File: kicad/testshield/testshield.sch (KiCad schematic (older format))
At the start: 6 parts, among them J1 ISP header, J2 Raspiheader, SW1 SW_Push, U1 ATMEGA328P-PU

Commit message: update
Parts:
- R1: footprint Resistors_THT:R_Axial_DIN0207_L6.3mm_D2.5mm_P10.16mm_Horizontal -> Resistors_SMD:R_2010
- U1: footprint ATMEGA328P-PU:DIP794W46P254L2967H457Q28B -> ATMEGA328P-AU:QFP80P900X900X120-32N
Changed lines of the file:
@@
 F 0 "U1" H 3200 4600 50  0000 L BNN
 F 1 "ATMEGA328P-PU" H 4350 1950 50  0000 L BNN
-F 2 "ATMEGA328P-PU:DIP794W46P254L2967H457Q28B" H 3950 3350 50  0001 C CIN
+F 2 "ATMEGA328P-AU:QFP80P900X900X120-32N" H 3950 3350 50  0001 C CIN
 F 3 "" H 3950 3350 50  0001 C CNN
 	1    3950 3350
@@
 F 0 "R1" V 6130 3250 50  0000 C CNN
 F 1 "10k" V 6050 3250 50  0000 C CNN
-F 2 "Resistors_THT:R_Axial_DIN0207_L6.3mm_D2.5mm_P10.16mm_Horizontal" V 5980 3250 50  0001 C CNN
+F 2 "Resistors_SMD:R_2010" V 5980 3250 50  0001 C CNN
 F 3 "" H 6050 3250 50  0001 C CNN
 	1    6050 3250

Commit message: Add files via upload
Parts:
- removed J1: ISP header, Pin_Headers:Pin_Header_Straight_2x03_Pitch2.54mm, symbol Conn_02x03_Odd_Even
- removed R1: 10k, Resistors_SMD:R_2010, symbol R
- removed SW1: SW_Push, Buttons_Switches_SMD:SW_SPST_B3S-1000, symbol SW_Push
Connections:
- net +3V3: now also J2.17 (Pin_17); no longer J2.1 (Pin_1)
- net GNDD: now also J2.14 (Pin_14), J2.20 (Pin_20), J2.25 (Pin_25), J2.30 (Pin_30), J2.34 (Pin_34), J2.39 (Pin_39), J2.9 (Pin_9)
- net at U1.1 ((PCINT14/~RESET~)PC6): now also J2.26 (Pin_26)
- net at U1.16 ((PCINT2/OC1B/~SS~)PB2): now also J2.24 (Pin_24)
- net at U1.17 ((PCINT3/OC2A/MOSI)PB3): now also J2.19 (Pin_19)
- net at U1.18 ((PCINT4/MISO)PB4): now also J2.21 (Pin_21)
- net at U1.19 ((PCINT5/SCK)PB5): now also J2.23 (Pin_23)
- net at U1.2 ((PCINT16/RXD)PD0): now also J2.8 (Pin_8)
- net at U1.26 ((PCINT11/ADC3)PC3): now also J2.11 (Pin_11)
- net at U1.3 ((PCINT17/TXD)PD1): now also J2.10 (Pin_10)
- net at U1.5 ((PCINT19/OC2B/INT1)PD3): now also J2.32 (Pin_32)
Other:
- moved on the sheet: J2

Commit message: Add files via upload
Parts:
- added D1: LED1, LEDs:LED_0603, symbol LED
- added D2: LED2, LEDs:LED_0603, symbol LED
- added J1: ISP/PDI, Pin_Headers:Pin_Header_Straight_2x03_Pitch2.54mm, symbol Conn_02x03_Odd_Even
- added R1: 1k, Resistors_SMD:R_0603, symbol R
- added R2, R3: 330, Resistors_SMD:R_0603, symbol R
- added R4: 10k, Resistors_SMD:R_0603, symbol R
- added SW1: Reset, Buttons_Switches_SMD:SW_SPST_B3U-1000P, symbol SW_Push
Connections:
- wire segments 75 -> 99

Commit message: simplification of schema with labels, WIP
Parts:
- D1, D2: symbol LED -> LED-RESCUE-testshield
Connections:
- net labels added: 3V3, GND, MISO, MOSI, PWM, RST, RX, SCK, SCL, SDA, SS, TX
- wire segments 99 -> 75
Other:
- note added: "TX / RX based on Raspberry Pi pins"
- moved on the sheet: R2, R3, R4, SW1

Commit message: further simplification,  still WIP
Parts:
- added R? (x2): 2K7, symbol R
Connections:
- net +3V3: now also R?.1, R?.1
- net PWM: now also U1.24 ((PCINT9/ADC1)PC1)
- net SCL: now also R?.2
- net SDA: now also R?.2
- net GPIO23: now reaches U1.25 ((PCINT10/ADC2)PC2)
- net GPIO23: now also J2.16 (Pin_16)
- net GPIO17: now reaches J2.11 (Pin_11), U1.26 ((PCINT11/ADC3)PC3)
- net at U1.5 ((PCINT19/OC2B/INT1)PD3): no longer J2.32 (Pin_32)
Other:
- note added: "Power"
- note added: "Programming header"
- note added: "Pull-up resistors for i2c lines\n"
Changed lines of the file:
@@
 	-1   0    0    1
 $EndComp
-Text Label 5150 3500 2    60   ~ 0
+Text Label 5300 3500 2    60   ~ 0
 SDA
-Text Label 5150 3600 2    60   ~ 0
+Text Label 5300 3600 2    60   ~ 0
 SCL
 Text Label 6750 2700 0    60   ~ 0
@@
 	2700 2850 3050 2850
 Wire Wire Line
-	2700 1950 2700 2250
-Wire Wire Line
-	2700 2250 2700 2550
-Wire Wire Line
-	2700 2550 2700 2850
-Wire Wire Line
-	2700 2850 2700 3500
+	2700 1950 2700 3500
 Wire Wire Line
 	2700 2550 3050 2550
 Wire Wire Line
-	2200 2250 2700 2250
-Wire Wire Line
-	2700 2250 3050 2250
+	2200 2250 3050 2250
 Connection ~ 2700 2550
 Connection ~ 2700 2250
@@
 	3050 4450 2700 4450
 Wire Wire Line
-	2700 3800 2700 4450
-Wire Wire Line
-	2700 4450 2700 4550
-Wire Wire Line
-	2700 4550 2700 5000
-Wire Wire Line
-	2200 4550 2700 4550
-Wire Wire Line
-	2700 4550 3050 4550
+	2700 3800 2700 5000
+Wire Wire Line
+	2200 4550 3050 4550
 Connection ~ 2700 4550
 Connection ~ 2700 2850
 Connection ~ 2700 4450
 Wire Wire Line
-	6950 3000 6600 3000
-Wire Wire Line
-	6600 3000 6600 3200
-Wire Wire Line
-	6600 3200 5450 3200
-Wire Wire Line
-	5450 3200 5450 3400
-Wire Wire Line
-	5450 3400 4950 3400
-Wire Wire Line
-	7450 4000 7700 4000
-Wire Wire Line
-	7700 4000 7700 4600
-Wire Wire Line
-	7700 4600 6600 4600
-Wire Wire Line
-	6600 4600 6600 4150
-Wire Wire Line
-	6600 4150 4950 4150
+	6950 3000 6650 3000
+Wire Wire Line
+	5300 3400 4950 3400
 Wire Wire Line
 	7700 5600 7950 5600
@@
 	2200 3800 2200 4550
 Wire Wire Line
-	5350 850  5350 750
-Wire Wire Line
 	5100 5600 5250 5600
 Wire Wire Line
-	4950 3500 5150 3500
-Wire Wire Line
-	4950 3600 5150 3600
+	4950 3500 5300 3500
+Wire Wire Line
+	4950 3600 5300 3600
 Wire Wire Line
 	6950 2600 6750 2600
@@
 Wire Wire Line
 	7650 3600 7450 3600
-Text Label 5150 2450 2    60   ~ 0
+Text Label 5300 2450 2    60   ~ 0
 SS
 Wire Wire Line
-	5150 2450 4950 2450
+	5300 2450 4950 2450
 Wire Wire Line
 	6700 5050 6700 5300
 Wire Wire Line
-	6250 5600 6700 5600
-Wire Wire Line
-	6700 5600 6850 5600
+	6250 5600 6850 5600
 Connection ~ 6700 5600
 Text Label 6250 5600 0    60   ~ 0
 RST
-Text Label 5150 3700 2    60   ~ 0
+Text Label 5300 3700 2    60   ~ 0
 RST
 Text Label 7650 3700 2    60   ~ 0
@@
 	7650 3700 7450 3700
 Wire Wire Line
-	5150 3700 4950 3700
-Wire Wire Line
-	4950 2750 5150 2750
-Text Label 5150 2750 2    60   ~ 0
+	5300 3700 4950 3700
+Wire Wire Line
+	4950 2750 5300 2750
+Text Label 5300 2750 2    60   ~ 0
 SCK
 Wire Wire Line
@@
 Text Label 6750 3600 0    60   ~ 0
 SCK
-Text Label 5150 2550 2    60   ~ 0
+Text Label 5300 2550 2    60   ~ 0
 MOSI
-Text Label 5150 2650 2    60   ~ 0
+Text Label 5300 2650 2    60   ~ 0
 MISO
 Wire Wire Line
-	4950 2650 5150 2650
-Wire Wire Line
-	5150 2550 4950 2550
+	4950 2650 5300 2650
+Wire Wire Line
+	5300 2550 4950 2550
 Wire Wire Line
 	6950 3400 6750 3400
@@
 Text Label 7650 2900 2    60   ~ 0
 RX
-Text Notes 8500 2250 2    60   ~ 0
-TX / RX based on Raspberry Pi pins
-Text Label 5150 3850 2    60   ~ 0
+Text Label 5300 3850 2    60   ~ 0
 TX
-Text Label 5150 3950 2    60   ~ 0
+Text Label 5300 3950 2    60   ~ 0
 RX
 Wire Wire Line
-	5150 3950 4950 3950
-Wire Wire Line
-	5150 3850 4950 3850
+	5300 3950 4950 3950
+Wire Wire Line
+	5300 3850 4950 3850
 Wire Wire Line
 	7650 2800 7450 2800
@@
 	1    0    0    -1
 $EndComp
+Wire Wire Line
+	4950 3200 5300 3200
+Text Label 5300 3200 2    60   ~ 0
+PWM
+Text Label 5300 3400 2    60   ~ 0
+GPIO17
+Text Label 6650 3000 0    60   ~ 0
+GPIO17
+Text Label 7800 3200 2    60   ~ 0
+GPIO23
+Text Label 5300 3300 2    60   ~ 0
+GPIO23
+Wire Wire Line
+	7450 3200 7800 3200
+Wire Wire Line
+	4950 3300 5300 3300
+Text Notes 8500 2250 2    60   ~ 0
+TX / RX based on Raspberry Pi pins
+Wire Wire Line
+	1550 6250 1900 6250
+Wire Wire Line
+	1550 6700 1900 6700
+Text Label 1550 6250 0    60   ~ 0
+SDA
+Text Label 1550 6700 0    60   ~ 0
+SCL
+$Comp
+L R R?
+U 1 1 5ACE28B0
+P 2050 6250
+F 0 "R?" V 2130 6250 50  0000 C CNN
+F 1 "2K7" V 2050 6250 50  0000 C CNN
+F 2 "" V 1980 6250 50  0000 C CNN
+F 3 "" H 2050 6250 50  0000 C CNN
+	1    2050 6250
+	0    1    1    0
+$EndComp
+$Comp
+L R R?
+U 1 1 5ACE28ED
+P 2050 6700
+F 0 "R?" V 2130 6700 50  0000 C CNN
+F 1 "2K7" V 2050 6700 50  0000 C CNN
+F 2 "" V 1980 6700 50  0000 C CNN
+F 3 "" H 2050 6700 50  0000 C CNN
+	1    2050 6700
+	0    1    1    0
+$EndComp
+Wire Wire Line
+	2200 6250 2450 6250
+Wire Wire Line
+	2200 6700 2450 6700
+Text Label 2450 6250 2    60   ~ 0
+3V3
+Text Label 2450 6700 2    60   ~ 0
+3V3
+Text Notes 1300 6000 0    60   ~ 0
+Pull-up resistors for i2c lines\n
+Text Notes 5350 1100 0    60   ~ 0
+Programming header
+Text Notes 9150 2900 0    60   ~ 0
+Power
 $EndSCHEMATC

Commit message: pcb layout WIP
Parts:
- C1: footprint Capacitors_SMD:CP_Elec_3x5.3 -> Capacitors_SMD:c_elec_4x5.3
- D1, D2: footprint LEDs:LED_0603 -> LEDs:LED_0805
- J1: footprint Pin_Headers:Pin_Header_Straight_2x03_Pitch2.54mm -> Pin_Headers:Pin_Header_Straight_2x03
- J2: footprint Pin_Headers:Pin_Header_Straight_2x20_Pitch2.54mm -> Pin_Headers:Pin_Header_Straight_2x20
- R5, R6: renamed from R?; footprint (none) -> Resistors_SMD:R_0603
- SW1: footprint Buttons_Switches_SMD:SW_SPST_B3U-1000P -> Buttons_Switches_SMD:SW_SPST_B3SL-1022P
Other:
- note added: "Notification led"
- note added: "Reset button"
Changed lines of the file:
@@
 LIBS:contrib
 LIBS:valves
+LIBS:ATMEGA328P-AU
 LIBS:testshield-cache
 EELAYER 25 0
@@
 F 0 "C1" H 2725 3750 50  0000 L CNN
 F 1 "0.1u" H 2725 3550 50  0000 L CNN
-F 2 "Capacitors_SMD:CP_Elec_3x5.3" H 2700 3650 50  0001 C CNN
+F 2 "Capacitors_SMD:c_elec_4x5.3" H 2700 3650 50  0001 C CNN
 F 3 "" H 2700 3650 50  0001 C CNN
 	1    2700 3650
@@
 F 0 "J2" H 7200 4400 50  0000 C CNN
 F 1 "Raspiheader" H 7200 2300 50  0000 C CNN
-F 2 "Pin_Headers:Pin_Header_Straight_2x20_Pitch2.54mm" H 7150 3400 50  0001 C CNN
+F 2 "Pin_Headers:Pin_Header_Straight_2x20" H 7150 3400 50  0001 C CNN
 F 3 "" H 7150 3400 50  0001 C CNN
 	1    7150 3400
@@
 F 0 "J1" H 5800 1650 50  0000 C CNN
 F 1 "ISP/PDI" H 5800 1250 50  0000 C CNN
-F 2 "Pin_Headers:Pin_Header_Straight_2x03_Pitch2.54mm" H 5750 1450 50  0001 C CNN
+F 2 "Pin_Headers:Pin_Header_Straight_2x03" H 5750 1450 50  0001 C CNN
 F 3 "" H 5750 1450 50  0001 C CNN
 	1    5750 1450
@@
 F 0 "SW1" H 7100 5700 50  0000 L CNN
 F 1 "Reset" H 7050 5540 50  0000 C CNN
-F 2 "Buttons_Switches_SMD:SW_SPST_B3U-1000P" H 7050 5800 50  0001 C CNN
+F 2 "Buttons_Switches_SMD:SW_SPST_B3SL-1022P" H 7050 5800 50  0001 C CNN
 F 3 "" H 7050 5800 50  0001 C CNN
 	1    7050 5600
@@
 F 0 "D1" H 2200 3750 50  0000 C CNN
 F 1 "LED1" H 2200 3550 50  0000 C CNN
-F 2 "LEDs:LED_0603" H 2200 3650 50  0001 C CNN
+F 2 "LEDs:LED_0805" H 2200 3650 50  0001 C CNN
 F 3 "" H 2200 3650 50  0001 C CNN
 	1    2200 3650
@@
 F 0 "D2" H 5400 5700 50  0000 C CNN
 F 1 "LED2" H 5400 5500 50  0000 C CNN
-F 2 "LEDs:LED_0603" H 5400 5600 50  0001 C CNN
+F 2 "LEDs:LED_0805" H 5400 5600 50  0001 C CNN
 F 3 "" H 5400 5600 50  0001 C CNN
 	1    5400 5600
@@
 GND
 $Comp
-L GNDD #PWR?
+L GNDD #PWR03
 U 1 1 5ACE0E6A
 P 9400 3850
-F 0 "#PWR?" H 9400 3600 50  0001 C CNN
+F 0 "#PWR03" H 9400 3600 50  0001 C CNN
 F 1 "GNDD" H 9400 3700 50  0000 C CNN
 F 2 "" H 9400 3850 50  0000 C CNN
@@
 $EndComp
 $Comp
-L +3V3 #PWR?
+L +3V3 #PWR04
 U 1 1 5ACE0E94
 P 9400 3200
-F 0 "#PWR?" H 9400 3050 50  0001 C CNN
+F 0 "#PWR04" H 9400 3050 50  0001 C CNN
 F 1 "+3V3" H 9400 3340 50  0000 C CNN
 F 2 "" H 9400 3200 50  0000 C CNN
@@
 SCL
 $Comp
-L R R?
+L R R5
 U 1 1 5ACE28B0
 P 2050 6250
-F 0 "R?" V 2130 6250 50  0000 C CNN
+F 0 "R5" V 2130 6250 50  0000 C CNN
 F 1 "2K7" V 2050 6250 50  0000 C CNN
-F 2 "" V 1980 6250 50  0000 C CNN
+F 2 "Resistors_SMD:R_0603" V 1980 6250 50  0001 C CNN
 F 3 "" H 2050 6250 50  0000 C CNN
 	1    2050 6250
@@
 $EndComp
 $Comp
-L R R?
+L R R6
 U 1 1 5ACE28ED
 P 2050 6700
-F 0 "R?" V 2130 6700 50  0000 C CNN
+F 0 "R6" V 2130 6700 50  0000 C CNN
 F 1 "2K7" V 2050 6700 50  0000 C CNN
-F 2 "" V 1980 6700 50  0000 C CNN
+F 2 "Resistors_SMD:R_0603" V 1980 6700 50  0001 C CNN
 F 3 "" H 2050 6700 50  0000 C CNN
 	1    2050 6700
@@
 Text Notes 9150 2900 0    60   ~ 0
 Power
+Text Notes 6600 5950 0    60   ~ 0
+Reset button
+Text Notes 4950 5900 0    60   ~ 0
+Notification led
 $EndSCHEMATC

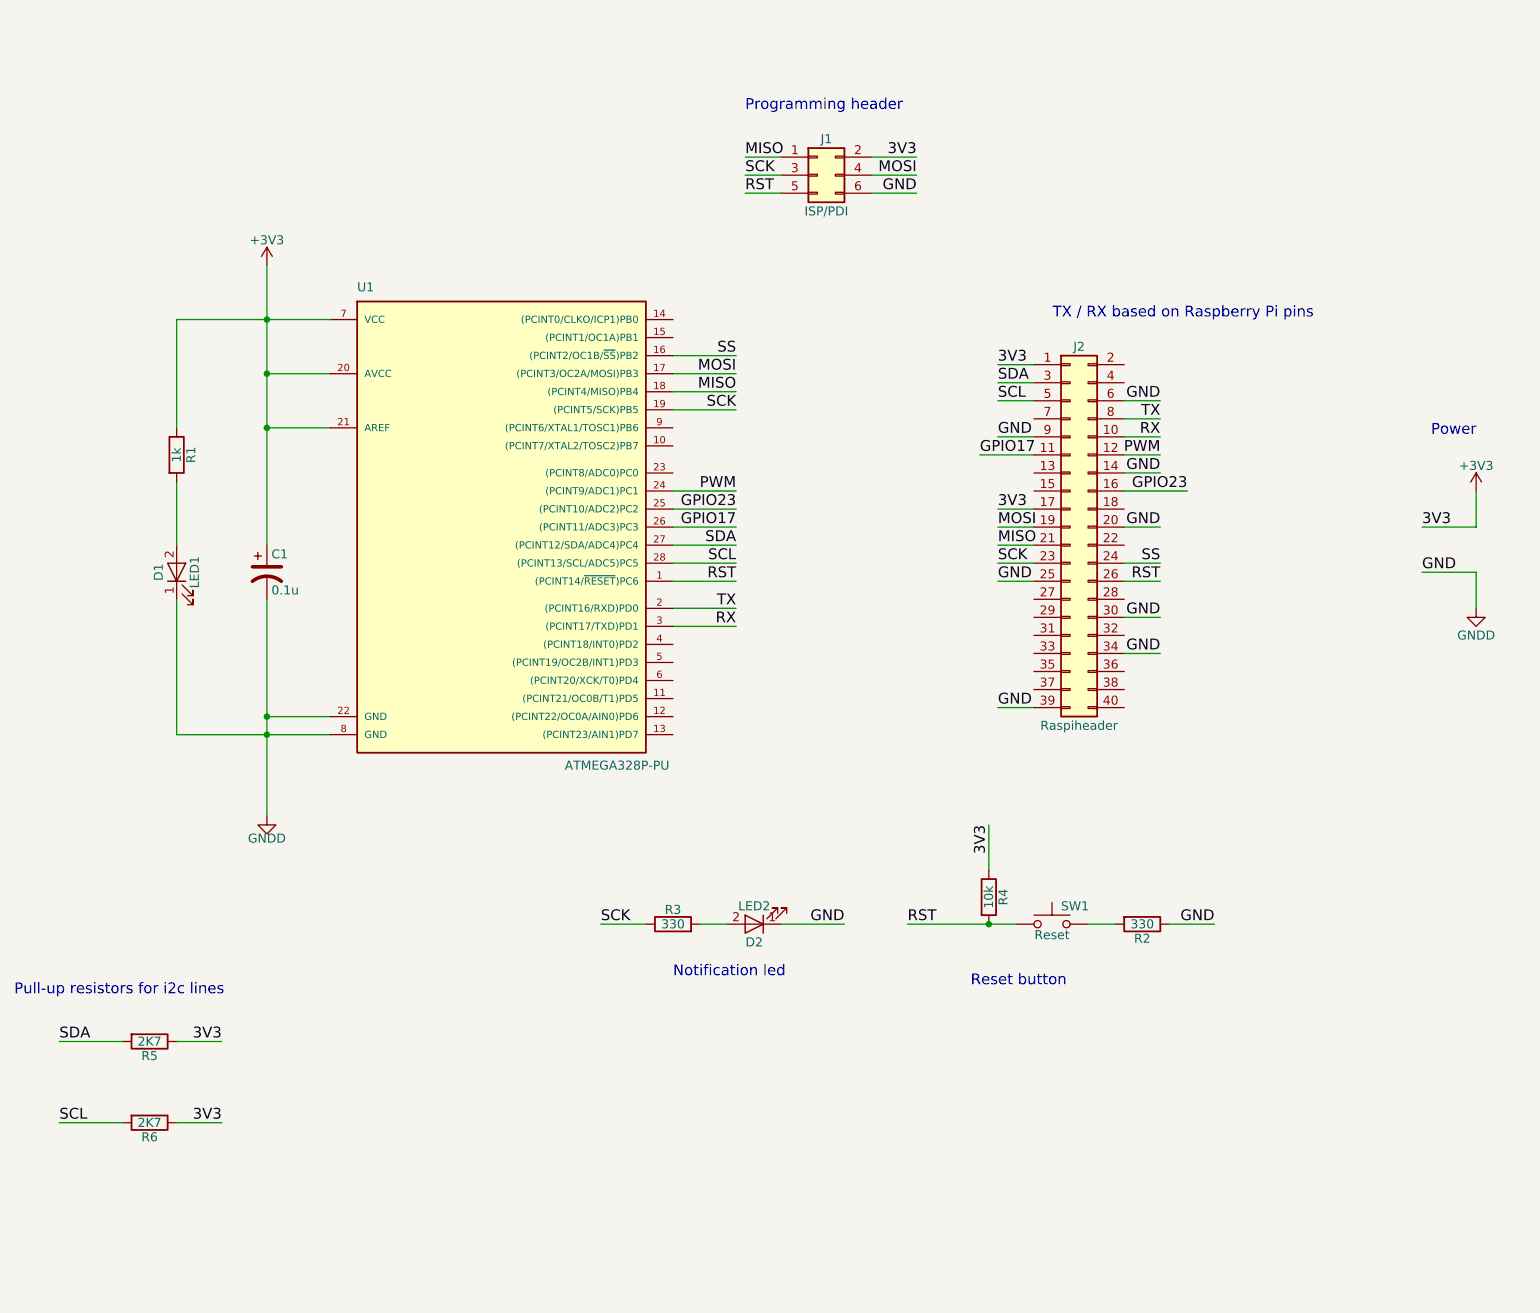
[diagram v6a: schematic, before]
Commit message: updated board
added decoupling caps
added miso mosi sck resistors
updated footprints
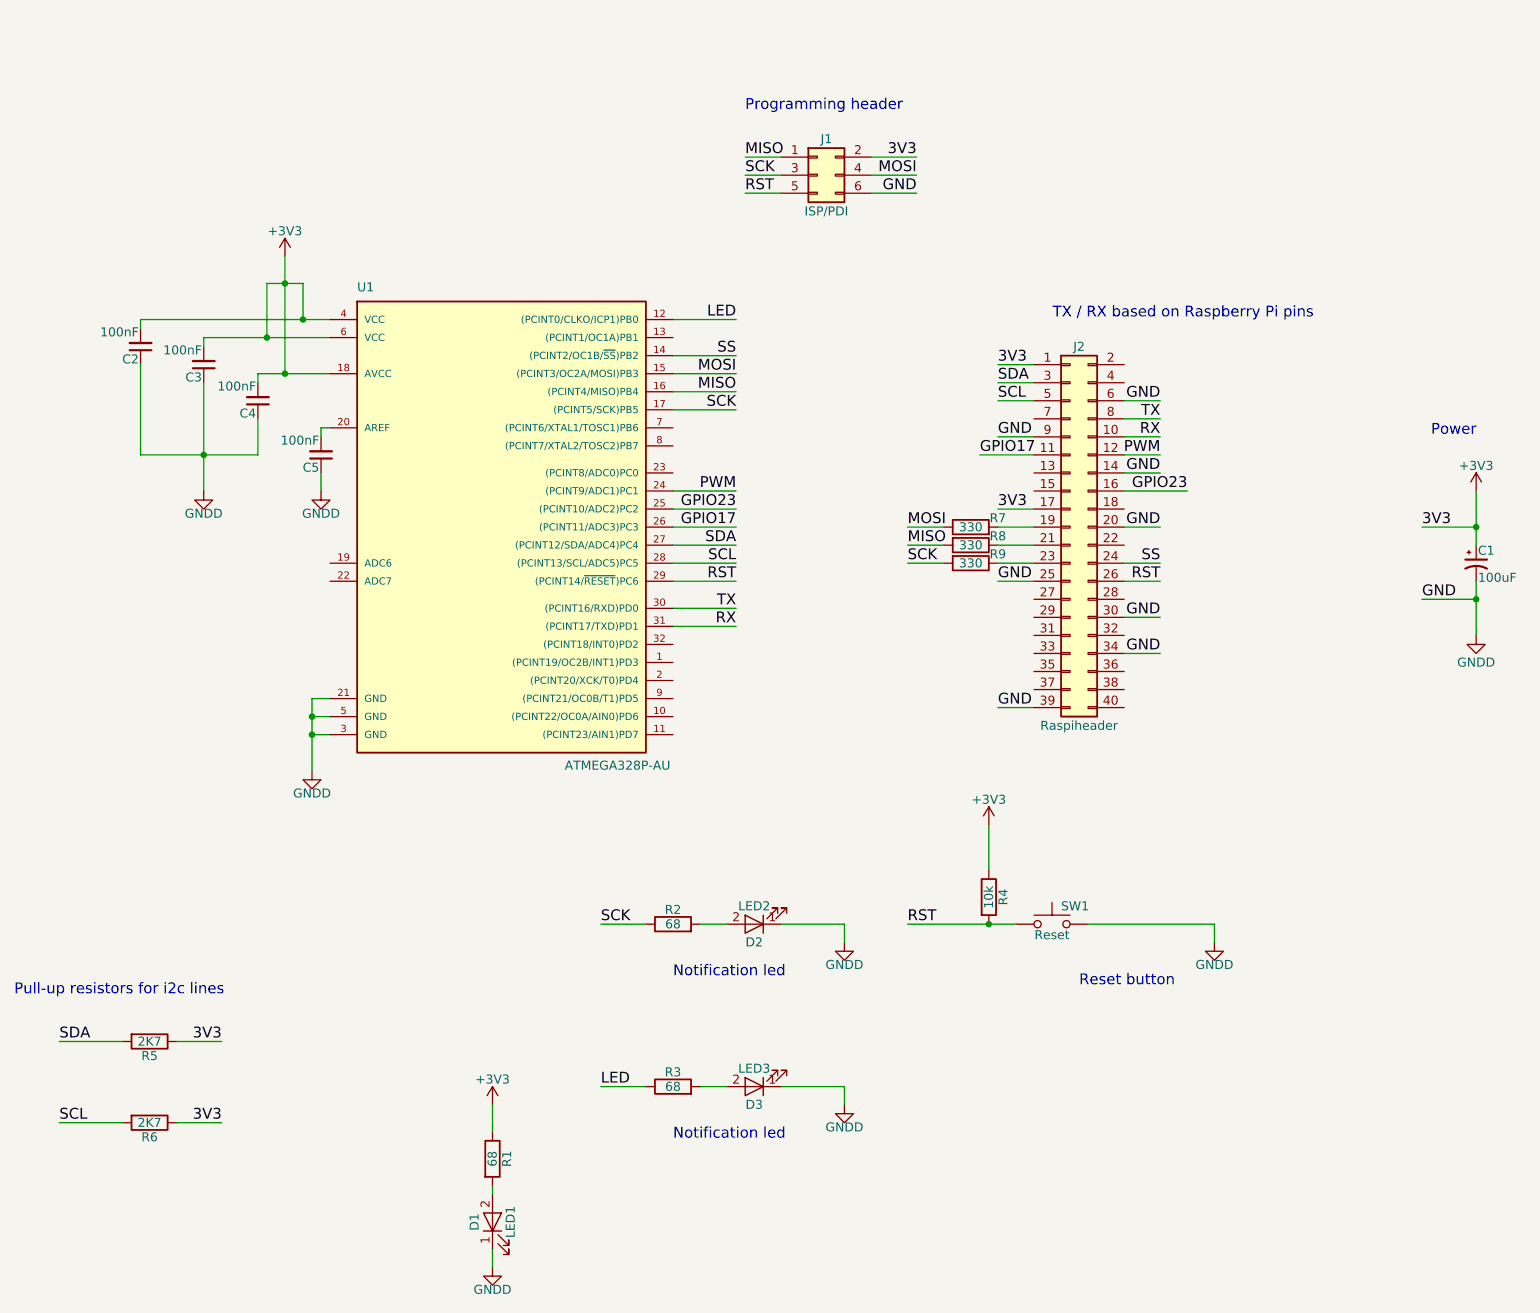
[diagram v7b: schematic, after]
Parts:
- removed C1: 0.1u, Capacitors_SMD:c_elec_4x5.3, symbol CP1
- removed R2: 330, Resistors_SMD:R_0603, symbol R
- removed U1: ATMEGA328P-PU, ATMEGA328P-AU:QFP80P900X900X120-32N, symbol ATMEGA328P-PU
- added C1: 100uF, Capacitors_Tantalum_SMD:CP_Tantalum_Case-D_EIA-7343-31_Hand, symbol CP1_Small
- added C2, C3, C4, C5: 100nF, Capacitors_SMD:C_0805_HandSoldering, symbol C_Small
- added D3: LED3, LEDs:LED_0805_HandSoldering, symbol LED-RESCUE-testshield
- added R3: 68, Resistors_SMD:R_0805_HandSoldering, symbol R
- added R7, R8, R9: 330, Resistors_SMD:R_0805_HandSoldering, symbol R
- added U1: ATMEGA328P-AU, Housings_QFP:TQFP-32_7x7mm_Pitch0.8mm, symbol ATMEGA328P-AU
- D1, D2: footprint LEDs:LED_0805 -> LEDs:LED_0805_HandSoldering
- R1: value 1k -> 68; footprint Resistors_SMD:R_0603 -> Resistors_SMD:R_0805_HandSoldering
- R2: renamed from R3; value 330 -> 68; footprint Resistors_SMD:R_0603 -> Resistors_SMD:R_0805_HandSoldering
- R4, R5, R6: footprint Resistors_SMD:R_0603 -> Resistors_SMD:R_0805_HandSoldering
- SW1: footprint Buttons_Switches_SMD:SW_SPST_B3SL-1022P -> Buttons_Switches_SMD:SW_SPST_B3S-1000
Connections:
- net +3V3: now also C1.1, C2.2, C3.2, C4.2, U1.18 (AVCC), U1.4 (VCC), U1.6 (VCC)
- net GNDD: now also SW1.2, C1.2, C2.1, C3.1, C4.1, C5.1, D3.1 (K), U1.21 (GND), U1.3 (GND), U1.5 (GND)
- net GPIO17: now also U1.26 ((PCINT11/ADC3)PC3)
- net GPIO23: now also U1.25 ((PCINT10/ADC2)PC2)
- net MISO: now also R8.2, U1.16 ((PCINT4/MISO)PB4); no longer J2.21 (Pin_21)
- net MOSI: now also R7.1, U1.15 ((PCINT3/OC2A/MOSI)PB3); no longer J2.19 (Pin_19)
- net PWM: now also U1.24 ((PCINT9/ADC1)PC1)
- net RST: now also U1.29 ((PCINT14/~RESET~)PC6)
- net RX: now also U1.31 ((PCINT17/TXD)PD1)
- net SCK: now also R9.2, U1.17 ((PCINT5/SCK)PB5); no longer J2.23 (Pin_23)
- net SCL: now also U1.28 ((PCINT13/SCL/ADC5)PC5)
- net SDA: now also U1.27 ((PCINT12/SDA/ADC4)PC4)
- net SS: now also U1.14 ((PCINT2/OC1B/~SS~)PB2)
- net TX: now also U1.30 ((PCINT16/RXD)PD0)
- new net: J2.19 (Pin_19), R7.2
- new net: J2.21 (Pin_21), R8.1
- new net: J2.23 (Pin_23), R9.1
- new net: C5.2, U1.20 (AREF)
- new net: D3.2 (A), R3.2
- new net LED: R3.1, U1.12 ((PCINT0/CLKO/ICP1)PB0)
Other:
- moved on the sheet: D1, R1

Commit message: created layout PDFs
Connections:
- net PWMa: now reaches U1.1 ((PCINT19/OC2B/INT1)PD3)
- net PWMa: now also J2.16 (Pin_16)
- net GPIO23 renamed PWMp
- net PWMp: now also J2.12 (Pin_12); no longer J2.16 (Pin_16)
- net PWM: no longer names the net of U1.24 ((PCINT9/ADC1)PC1)
- net PWM: no longer J2.12 (Pin_12)
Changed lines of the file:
@@
 RX
 Text Label 7650 3000 2    60   ~ 0
-PWM
+PWMp
 Text Label 9100 3400 0    60   ~ 0
 3V3
@@
 	1    0    0    -1
 $EndComp
-Text Label 5300 3200 2    60   ~ 0
-PWM
+Text Label 5300 3300 2    60   ~ 0
+PWMp
 Text Label 5300 3400 2    60   ~ 0
 GPIO17
@@
 GPIO17
 Text Label 7800 3200 2    60   ~ 0
-GPIO23
-Text Label 5300 3300 2    60   ~ 0
-GPIO23
+PWMa
 Text Notes 8500 2250 2    60   ~ 0
 TX / RX based on Raspberry Pi pins
@@
 	9400 3700 9400 4000
 Wire Wire Line
-	4950 3200 5300 3200
-Wire Wire Line
 	7450 3200 7800 3200
-Wire Wire Line
-	4950 3300 5300 3300
 Wire Wire Line
 	1550 6250 1900 6250
@@
 Wire Wire Line
 	5900 6500 5900 6600
+Wire Wire Line
+	4950 4150 5300 4150
+Text Label 5300 4150 2    60   ~ 0
+PWMa
+Wire Wire Line
+	4950 3300 5300 3300
 $EndSCHEMATC
